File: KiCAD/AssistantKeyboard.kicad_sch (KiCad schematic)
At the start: 14 parts, among them J1 Conn_01x04_Male, J2 Conn_01x12_Male, J3 Conn_01x12_Male, J4 Conn_01x02_Male, SW1 SW_Push, SW13 RotaryEncoder_Switch, SW2 SW_Push, SW3 SW_Push, SW4 SW_Push, SW5 SW_Push, SW6 SW_Push, SW7 SW_Push, SW8 SW_Push, SW9 SW_Push

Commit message: Naming PCB files, code improvements
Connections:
- net D15: no longer names the net of J3.9 (Pin_9)
- net D9: no longer names the net of J2.1 (Pin_1)
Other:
- title: (none) -> AssistantKeyboard
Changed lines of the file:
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@@
 (kicad_sch (version 20211123) (generator eeschema)
   (paper "A4")
+  (title_block
+    (title "AssistantKeyboard")
+    (date "2022-02-26")
+    (rev "0.9")
+  )
   (junction (at 76.2 95.25) (diameter 0) (color 0 0 0 0)
   )
@@
   (junction (at 64.77 91.44) (diameter 0) (color 0 0 0 0)
   )
+  (junction (at 48.26 111.76) (diameter 0) (color 0 0 0 0)
+  )
   (junction (at 48.26 95.25) (diameter 0) (color 0 0 0 0)
   )
-  (junction (at 48.26 111.76) (diameter 0) (color 0 0 0 0)
-  )
-  (junction (at 48.26 107.95) (diameter 0) (color 0 0 0 0)
-  )
+  (no_connect (at 111.76 62.23))
+  (no_connect (at 125.73 54.61))
   (no_connect (at 125.73 34.29))
   (no_connect (at 111.76 52.07))
@@
   (no_connect (at 125.73 46.99))
   (no_connect (at 128.27 41.91))
-  (no_connect (at 133.35 90.17))
-  (no_connect (at 43.18 142.24))
   (wire (pts (xy 52.07 171.45) (xy 71.12 171.45))
     (stroke (width 0) (type default) (color 0 0 0 0))
@@
     (stroke (width 0) (type default) (color 0 0 0 0))
   )
-  (wire (pts (xy 133.35 86.36) (xy 133.35 90.17))
-    (stroke (width 0) (type default) (color 0 0 0 0))
-  )
   (wire (pts (xy 76.2 95.25) (xy 104.14 95.25))
     (stroke (width 0) (type default) (color 0 0 0 0))
@@
     (stroke (width 0) (type default) (color 0 0 0 0))
   )
+  (wire (pts (xy 48.26 111.76) (xy 76.2 111.76))
+    (stroke (width 0) (type default) (color 0 0 0 0))
+  )
   (wire (pts (xy 86.36 171.45) (xy 92.71 171.45))
     (stroke (width 0) (type default) (color 0 0 0 0))
@@
     (stroke (width 0) (type default) (color 0 0 0 0))
   )
-  (wire (pts (xy 48.26 111.76) (xy 76.2 111.76))
-    (stroke (width 0) (type default) (color 0 0 0 0))
-  )
-  (wire (pts (xy 39.37 142.24) (xy 43.18 142.24))
-    (stroke (width 0) (type default) (color 0 0 0 0))
-  )
   (wire (pts (xy 48.26 95.25) (xy 76.2 95.25))
     (stroke (width 0) (type default) (color 0 0 0 0))
@@
     (stroke (width 0) (type default) (color 0 0 0 0))
   )
-  (wire (pts (xy 49.53 107.95) (xy 48.26 107.95))
-    (stroke (width 0) (type default) (color 0 0 0 0))
-  )
   (wire (pts (xy 39.37 128.27) (xy 46.99 128.27))
     (stroke (width 0) (type default) (color 0 0 0 0))
@@
     )
   )
-  (global_label "D9" (shape bidirectional) (at 111.76 62.23 180) (fields_autoplaced)
-    (effects (font (size 1.27 1.27)) (justify right))
-    (property "Intersheet References" "${INTERSHEET_REFS}" (id 0) (at 106.8674 62.1506 0)
-      (effects (font (size 1.27 1.27)) (justify right) hide)
-    )
-  )
   (global_label "D0" (shape input) (at 111.76 36.83 180) (fields_autoplaced)
     (effects (font (size 1.27 1.27)) (justify right))
@@
     )
   )
-  (global_label "D15" (shape bidirectional) (at 133.35 86.36 90) (fields_autoplaced)
-    (effects (font (size 1.27 1.27)) (justify left))
-    (property "Intersheet References" "${INTERSHEET_REFS}" (id 0) (at 133.2706 80.2579 90)
-      (effects (font (size 1.27 1.27)) (justify left) hide)
-    )
-  )
   (global_label "D6" (shape bidirectional) (at 39.37 95.25 180) (fields_autoplaced)
     (effects (font (size 1.27 1.27)) (justify right))
@@
     )
   )
-  (global_label "D9" (shape bidirectional) (at 39.37 142.24 180) (fields_autoplaced)
-    (effects (font (size 1.27 1.27)) (justify right))
-    (property "Intersheet References" "${INTERSHEET_REFS}" (id 0) (at 34.4774 142.1606 0)
-      (effects (font (size 1.27 1.27)) (justify right) hide)
-    )
-  )
   (global_label "D7" (shape bidirectional) (at 111.76 57.15 180) (fields_autoplaced)
     (effects (font (size 1.27 1.27)) (justify right))
@@
       (effects (font (size 1.27 1.27)) (justify left) hide)
     )
-  )
-  (global_label "D15" (shape bidirectional) (at 125.73 54.61 0) (fields_autoplaced)
-    (effects (font (size 1.27 1.27)) (justify left))
-    (property "Intersheet References" "${INTERSHEET_REFS}" (id 0) (at 131.8321 54.5306 0)
-      (effects (font (size 1.27 1.27)) (justify left) hide)
-    )

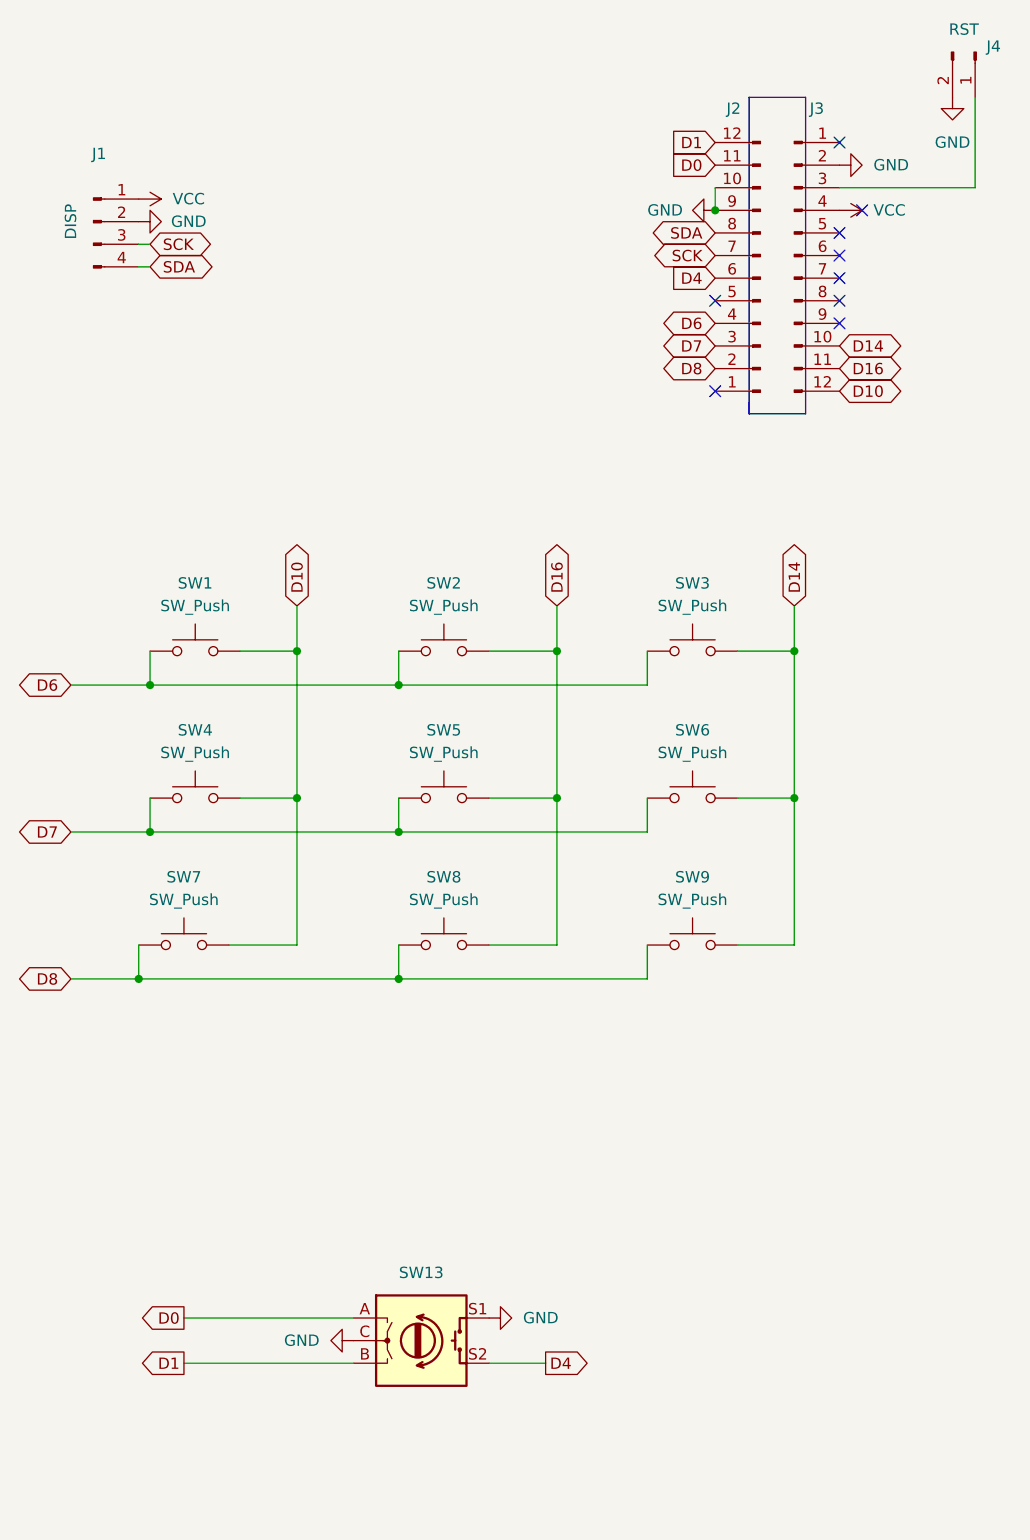
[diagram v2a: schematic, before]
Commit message: Debounce caps
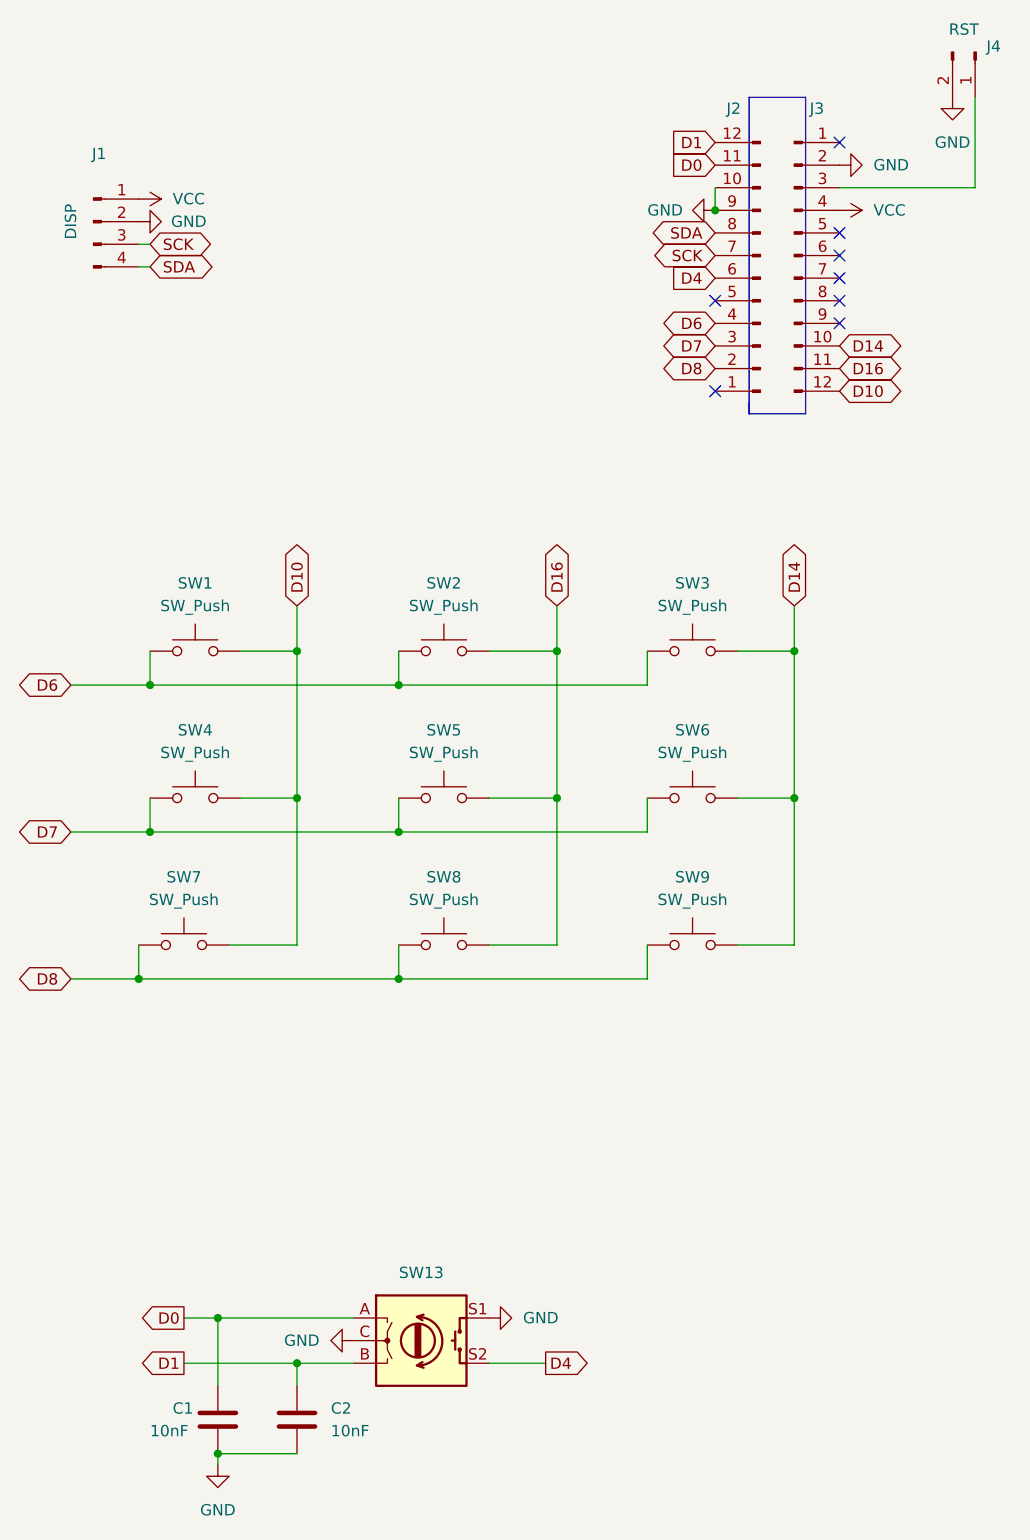
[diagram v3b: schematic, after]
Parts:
- added C1, C2: 10nF, Capacitor_SMD:C_0805_2012Metric_Pad1.18x1.45mm_HandSolder, symbol Device:C
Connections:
- net D0: now also C1.1
- net D1: now also C2.1
- net GND: now also C1.2, C2.2
- no-connect marks 9 -> 8
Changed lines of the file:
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@@
   (junction (at 93.98 107.95) (diameter 0) (color 0 0 0 0)
   )
+  (junction (at 55.88 166.37) (diameter 0) (color 0 0 0 0)
+  )
   (junction (at 111.76 41.91) (diameter 0) (color 0 0 0 0)
   )
@@
   (junction (at 64.77 107.95) (diameter 0) (color 0 0 0 0)
   )
+  (junction (at 64.77 171.45) (diameter 0) (color 0 0 0 0)
+  )
   (junction (at 120.65 91.44) (diameter 0) (color 0 0 0 0)
   )
@@
   )
   (junction (at 48.26 95.25) (diameter 0) (color 0 0 0 0)
+  )
+  (junction (at 55.88 181.61) (diameter 0) (color 0 0 0 0)
   )
   (no_connect (at 111.76 62.23))
@@
   (no_connect (at 125.73 44.45))
   (no_connect (at 125.73 46.99))
-  (no_connect (at 128.27 41.91))
-  (wire (pts (xy 52.07 171.45) (xy 71.12 171.45))
+  (wire (pts (xy 52.07 171.45) (xy 64.77 171.45))
     (stroke (width 0) (type default) (color 0 0 0 0))
   )
@@
     (stroke (width 0) (type default) (color 0 0 0 0))
   )
+  (wire (pts (xy 55.88 181.61) (xy 55.88 182.88))
+    (stroke (width 0) (type default) (color 0 0 0 0))
+  )
   (wire (pts (xy 140.97 39.37) (xy 125.73 39.37))
     (stroke (width 0) (type default) (color 0 0 0 0))
@@
     (stroke (width 0) (type default) (color 0 0 0 0))
   )
-  (wire (pts (xy 52.07 166.37) (xy 71.12 166.37))
+  (wire (pts (xy 52.07 166.37) (xy 55.88 166.37))
     (stroke (width 0) (type default) (color 0 0 0 0))
   )
@@
     (stroke (width 0) (type default) (color 0 0 0 0))
   )
+  (wire (pts (xy 64.77 171.45) (xy 64.77 173.99))
+    (stroke (width 0) (type default) (color 0 0 0 0))
+  )
   (wire (pts (xy 64.77 86.36) (xy 64.77 91.44))
     (stroke (width 0) (type default) (color 0 0 0 0))
@@
     (stroke (width 0) (type default) (color 0 0 0 0))
   )
+  (wire (pts (xy 55.88 181.61) (xy 64.77 181.61))
+    (stroke (width 0) (type default) (color 0 0 0 0))
+  )
   (wire (pts (xy 46.99 124.46) (xy 46.99 128.27))
     (stroke (width 0) (type default) (color 0 0 0 0))
@@
     (stroke (width 0) (type default) (color 0 0 0 0))
   )
+  (wire (pts (xy 64.77 171.45) (xy 71.12 171.45))
+    (stroke (width 0) (type default) (color 0 0 0 0))
+  )
   (wire (pts (xy 114.3 91.44) (xy 120.65 91.44))
     (stroke (width 0) (type default) (color 0 0 0 0))
@@
     (stroke (width 0) (type default) (color 0 0 0 0))
   )
+  (wire (pts (xy 55.88 166.37) (xy 55.88 173.99))
+    (stroke (width 0) (type default) (color 0 0 0 0))
+  )
   (wire (pts (xy 76.2 107.95) (xy 76.2 111.76))
     (stroke (width 0) (type default) (color 0 0 0 0))
@@
   )
   (wire (pts (xy 48.26 91.44) (xy 48.26 95.25))
+    (stroke (width 0) (type default) (color 0 0 0 0))
+  )
+  (wire (pts (xy 55.88 166.37) (xy 71.12 166.37))
     (stroke (width 0) (type default) (color 0 0 0 0))
   )
@@
     (pin "2")
   )
+  (symbol (lib_id "Device:C") (at 64.77 177.8 0) (unit 1)
+    (in_bom yes) (on_board yes) (fields_autoplaced)
+    (property "Reference" "C2" (id 0) (at 68.58 176.5299 0)
+      (effects (font (size 1.27 1.27)) (justify left))
+    )
+    (property "Value" "10nF" (id 1) (at 68.58 179.0699 0)
+      (effects (font (size 1.27 1.27)) (justify left))
+    )
+    (property "Footprint" "Capacitor_SMD:C_0805_2012Metric_Pad1.18x1.45mm_HandSolder" (id 2) (at 65.7352 181.61 0)
+      (effects (font (size 1.27 1.27)) hide)
+    )
+    (property "Datasheet" "~" (id 3) (at 64.77 177.8 0)
+      (effects (font (size 1.27 1.27)) hide)
+    )
+    (pin "1")
+    (pin "2")
+  )
   (symbol (lib_id "power:VCC") (at 125.73 41.91 270) (unit 1)
     (in_bom yes) (on_board yes) (fields_autoplaced)
@@
     )
     (pin "1")
+  )
+  (symbol (lib_id "Device:C") (at 55.88 177.8 0) (unit 1)
+    (in_bom yes) (on_board yes)
+    (property "Reference" "C1" (id 0) (at 50.8 176.53 0)
+      (effects (font (size 1.27 1.27)) (justify left))
+    )
+    (property "Value" "10nF" (id 1) (at 48.26 179.07 0)
+      (effects (font (size 1.27 1.27)) (justify left))
+    )
+    (property "Footprint" "Capacitor_SMD:C_0805_2012Metric_Pad1.18x1.45mm_HandSolder" (id 2) (at 56.8452 181.61 0)
+      (effects (font (size 1.27 1.27)) hide)
+    )
+    (property "Datasheet" "~" (id 3) (at 55.88 177.8 0)
+      (effects (font (size 1.27 1.27)) hide)
+    )
+    (pin "1")
+    (pin "2")
   )
   (symbol (lib_id "power:VCC") (at 46.99 40.64 270) (unit 1)
@@
     (pin "2")
   )
+  (symbol (lib_id "power:GND") (at 55.88 182.88 0) (unit 1)
+    (in_bom yes) (on_board yes) (fields_autoplaced)
+    (property "Reference" "#PWR0103" (id 0) (at 55.88 189.23 0)
+      (effects (font (size 1.27 1.27)) hide)
+    )
+    (property "Value" "GND" (id 1) (at 55.88 187.96 0))
+    (property "Footprint" "" (id 2) (at 55.88 182.88 0)
+      (effects (font (size 1.27 1.27)) hide)
+    )
+    (property "Datasheet" "" (id 3) (at 55.88 182.88 0)
+      (effects (font (size 1.27 1.27)) hide)
+    )
+    (pin "1")
+  )
   (symbol (lib_id "power:GND") (at 125.73 36.83 90) (unit 1)
     (in_bom yes) (on_board yes) (fields_autoplaced)
@@
       (reference "#PWR0102") (unit 1) (value "GND") (footprint "")
     )
+    (path "/eabf26cb-e3ea-4f34-b84a-b2b25e8b001a"
+      (reference "#PWR0103") (unit 1) (value "GND") (footprint "")
+    )
+    (path "/36cad135-112c-4600-939d-93f9eed314a3"
+      (reference "C1") (unit 1) (value "10nF") (footprint "Capacitor_SMD:C_0805_2012Metric_Pad1.18x1.45mm_HandSolder")
+    )
+    (path "/21139fd5-2600-4f3b-8ffa-de1972f9dc50"
+      (reference "C2") (unit 1) (value "10nF") (footprint "Capacitor_SMD:C_0805_2012Metric_Pad1.18x1.45mm_HandSolder")
+    )
     (path "/42c10b01-6c7e-49cb-afc3-d9f6b1686a0d"
